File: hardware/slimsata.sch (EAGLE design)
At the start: 2 parts

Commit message: Signaleitungen geroutet
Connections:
- removed net N$1: CON1G$2.GND1, CON1G$2.GND2, CON1G$2.GND3, CON1G$2.GND4, CON1G$2.GND5, CON1G$3.MECH1, CON1G$3.MECH2, CON2G$2.GND1, CON2G$2.GND2, CON2G$3.MECH1, CON2G$3.MECH2, CON2G$3.MECH3
- removed net N$2: CON1G$1.GND1, CON1G$1.GND2, CON1G$1.GND3, CON2G$1.GND1, CON2G$1.GND2, CON2G$1.GND3
- new net GND: CON1G$1.GND1, CON1G$1.GND2, CON1G$1.GND3, CON1G$2.GND1, CON1G$2.GND2, CON1G$2.GND3, CON1G$2.GND4, CON1G$2.GND5, CON1G$3.MECH1, CON1G$3.MECH2, CON2G$1.GND1, CON2G$1.GND2, CON2G$1.GND3, CON2G$2.GND1, CON2G$2.GND2, CON2G$3.MECH1, CON2G$3.MECH2, CON2G$3.MECH3
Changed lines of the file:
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@@
 </busses>
 <nets>
-<net name="N$1" class="0">
-<segment>
-<pinref part="CON1" gate="G$3" pin="MECH2"/>
-<wire x1="30.48" y1="17.78" x2="30.48" y2="15.24" width="0.1524" layer="91"/>
-<wire x1="30.48" y1="15.24" x2="30.48" y2="12.7" width="0.1524" layer="91"/>
-<wire x1="30.48" y1="12.7" x2="30.48" y2="10.16" width="0.1524" layer="91"/>
-<wire x1="30.48" y1="10.16" x2="30.48" y2="7.62" width="0.1524" layer="91"/>
-<wire x1="30.48" y1="7.62" x2="17.78" y2="7.62" width="0.1524" layer="91"/>
-<pinref part="CON1" gate="G$3" pin="MECH1"/>
-<wire x1="17.78" y1="10.16" x2="30.48" y2="10.16" width="0.1524" layer="91"/>
-<junction x="30.48" y="10.16"/>
-<pinref part="CON2" gate="G$3" pin="MECH3"/>
-<wire x1="43.18" y1="12.7" x2="30.48" y2="12.7" width="0.1524" layer="91"/>
-<junction x="30.48" y="12.7"/>
-<pinref part="CON2" gate="G$3" pin="MECH2"/>
-<wire x1="43.18" y1="15.24" x2="30.48" y2="15.24" width="0.1524" layer="91"/>
-<junction x="30.48" y="15.24"/>
-<pinref part="CON2" gate="G$3" pin="MECH1"/>
-<wire x1="43.18" y1="17.78" x2="30.48" y2="17.78" width="0.1524" layer="91"/>
-<pinref part="CON1" gate="G$2" pin="GND1"/>
-<wire x1="17.78" y1="50.8" x2="30.48" y2="50.8" width="0.1524" layer="91"/>
-<wire x1="30.48" y1="50.8" x2="30.48" y2="48.26" width="0.1524" layer="91"/>
-<junction x="30.48" y="17.78"/>
-<pinref part="CON1" gate="G$2" pin="GND2"/>
-<wire x1="30.48" y1="48.26" x2="30.48" y2="45.72" width="0.1524" layer="91"/>
-<wire x1="30.48" y1="45.72" x2="30.48" y2="40.64" width="0.1524" layer="91"/>
-<wire x1="30.48" y1="40.64" x2="30.48" y2="38.1" width="0.1524" layer="91"/>
-<wire x1="30.48" y1="38.1" x2="30.48" y2="35.56" width="0.1524" layer="91"/>
-<wire x1="30.48" y1="35.56" x2="30.48" y2="30.48" width="0.1524" layer="91"/>
-<wire x1="30.48" y1="30.48" x2="30.48" y2="17.78" width="0.1524" layer="91"/>
-<wire x1="17.78" y1="48.26" x2="30.48" y2="48.26" width="0.1524" layer="91"/>
-<junction x="30.48" y="48.26"/>
-<pinref part="CON1" gate="G$2" pin="GND3"/>
-<wire x1="17.78" y1="45.72" x2="30.48" y2="45.72" width="0.1524" layer="91"/>
-<junction x="30.48" y="45.72"/>
-<pinref part="CON1" gate="G$2" pin="GND4"/>
-<wire x1="17.78" y1="35.56" x2="30.48" y2="35.56" width="0.1524" layer="91"/>
-<junction x="30.48" y="35.56"/>
-<pinref part="CON1" gate="G$2" pin="GND5"/>
-<wire x1="17.78" y1="30.48" x2="30.48" y2="30.48" width="0.1524" layer="91"/>
-<junction x="30.48" y="30.48"/>
-<pinref part="CON2" gate="G$2" pin="GND2"/>
-<wire x1="43.18" y1="38.1" x2="30.48" y2="38.1" width="0.1524" layer="91"/>
-<junction x="30.48" y="38.1"/>
-<pinref part="CON2" gate="G$2" pin="GND1"/>
-<wire x1="43.18" y1="40.64" x2="30.48" y2="40.64" width="0.1524" layer="91"/>
-<junction x="30.48" y="40.64"/>
-</segment>
-</net>
-<net name="N$2" class="0">
-<segment>
-<pinref part="CON2" gate="G$1" pin="GND1"/>
-<pinref part="CON1" gate="G$1" pin="GND1"/>
-<wire x1="17.78" y1="81.28" x2="30.48" y2="81.28" width="0.1524" layer="91"/>
-<pinref part="CON1" gate="G$1" pin="GND2"/>
-<pinref part="CON2" gate="G$1" pin="GND2"/>
-<wire x1="30.48" y1="81.28" x2="43.18" y2="81.28" width="0.1524" layer="91"/>
-<wire x1="17.78" y1="73.66" x2="30.48" y2="73.66" width="0.1524" layer="91"/>
-<wire x1="30.48" y1="73.66" x2="43.18" y2="73.66" width="0.1524" layer="91"/>
-<wire x1="30.48" y1="81.28" x2="30.48" y2="73.66" width="0.1524" layer="91"/>
-<junction x="30.48" y="81.28"/>
-<junction x="30.48" y="73.66"/>
-<pinref part="CON1" gate="G$1" pin="GND3"/>
-<pinref part="CON2" gate="G$1" pin="GND3"/>
-<wire x1="17.78" y1="66.04" x2="30.48" y2="66.04" width="0.1524" layer="91"/>
-<wire x1="30.48" y1="66.04" x2="43.18" y2="66.04" width="0.1524" layer="91"/>
-<wire x1="30.48" y1="73.66" x2="30.48" y2="66.04" width="0.1524" layer="91"/>
-<junction x="30.48" y="66.04"/>
-</segment>
-</net>
 <net name="N$5" class="0">
 <segment>
@@
 </segment>
 </net>
+<net name="GND" class="0">
+<segment>
+<pinref part="CON2" gate="G$1" pin="GND1"/>
+<pinref part="CON1" gate="G$1" pin="GND1"/>
+<wire x1="17.78" y1="81.28" x2="30.48" y2="81.28" width="0.1524" layer="91"/>
+<pinref part="CON1" gate="G$1" pin="GND2"/>
+<pinref part="CON2" gate="G$1" pin="GND2"/>
+<wire x1="30.48" y1="81.28" x2="43.18" y2="81.28" width="0.1524" layer="91"/>
+<wire x1="17.78" y1="73.66" x2="30.48" y2="73.66" width="0.1524" layer="91"/>
+<wire x1="30.48" y1="73.66" x2="43.18" y2="73.66" width="0.1524" layer="91"/>
+<wire x1="30.48" y1="81.28" x2="30.48" y2="73.66" width="0.1524" layer="91"/>
+<junction x="30.48" y="81.28"/>
+<junction x="30.48" y="73.66"/>
+<pinref part="CON1" gate="G$1" pin="GND3"/>
+<pinref part="CON2" gate="G$1" pin="GND3"/>
+<wire x1="17.78" y1="66.04" x2="30.48" y2="66.04" width="0.1524" layer="91"/>
+<wire x1="30.48" y1="66.04" x2="43.18" y2="66.04" width="0.1524" layer="91"/>
+<wire x1="30.48" y1="73.66" x2="30.48" y2="66.04" width="0.1524" layer="91"/>
+<junction x="30.48" y="66.04"/>
+<pinref part="CON1" gate="G$3" pin="MECH2"/>
+<wire x1="30.48" y1="17.78" x2="30.48" y2="15.24" width="0.1524" layer="91"/>
+<wire x1="30.48" y1="15.24" x2="30.48" y2="12.7" width="0.1524" layer="91"/>
+<wire x1="30.48" y1="12.7" x2="30.48" y2="10.16" width="0.1524" layer="91"/>
+<wire x1="30.48" y1="10.16" x2="30.48" y2="7.62" width="0.1524" layer="91"/>
+<wire x1="30.48" y1="7.62" x2="17.78" y2="7.62" width="0.1524" layer="91"/>
+<pinref part="CON1" gate="G$3" pin="MECH1"/>
+<wire x1="17.78" y1="10.16" x2="30.48" y2="10.16" width="0.1524" layer="91"/>
+<junction x="30.48" y="10.16"/>
+<pinref part="CON2" gate="G$3" pin="MECH3"/>
+<wire x1="43.18" y1="12.7" x2="30.48" y2="12.7" width="0.1524" layer="91"/>
+<junction x="30.48" y="12.7"/>
+<pinref part="CON2" gate="G$3" pin="MECH2"/>
+<wire x1="43.18" y1="15.24" x2="30.48" y2="15.24" width="0.1524" layer="91"/>
+<junction x="30.48" y="15.24"/>
+<pinref part="CON2" gate="G$3" pin="MECH1"/>
+<wire x1="43.18" y1="17.78" x2="30.48" y2="17.78" width="0.1524" layer="91"/>
+<pinref part="CON1" gate="G$2" pin="GND1"/>
+<wire x1="17.78" y1="50.8" x2="30.48" y2="50.8" width="0.1524" layer="91"/>
+<wire x1="30.48" y1="50.8" x2="30.48" y2="48.26" width="0.1524" layer="91"/>
+<junction x="30.48" y="17.78"/>
+<pinref part="CON1" gate="G$2" pin="GND2"/>
+<wire x1="30.48" y1="48.26" x2="30.48" y2="45.72" width="0.1524" layer="91"/>
+<wire x1="30.48" y1="45.72" x2="30.48" y2="40.64" width="0.1524" layer="91"/>
+<wire x1="30.48" y1="40.64" x2="30.48" y2="38.1" width="0.1524" layer="91"/>
+<wire x1="30.48" y1="38.1" x2="30.48" y2="35.56" width="0.1524" layer="91"/>
+<wire x1="30.48" y1="35.56" x2="30.48" y2="30.48" width="0.1524" layer="91"/>
+<wire x1="30.48" y1="30.48" x2="30.48" y2="17.78" width="0.1524" layer="91"/>
+<wire x1="17.78" y1="48.26" x2="30.48" y2="48.26" width="0.1524" layer="91"/>
+<junction x="30.48" y="48.26"/>
+<pinref part="CON1" gate="G$2" pin="GND3"/>
+<wire x1="17.78" y1="45.72" x2="30.48" y2="45.72" width="0.1524" layer="91"/>
+<junction x="30.48" y="45.72"/>
+<pinref part="CON1" gate="G$2" pin="GND4"/>
+<wire x1="17.78" y1="35.56" x2="30.48" y2="35.56" width="0.1524" layer="91"/>
+<junction x="30.48" y="35.56"/>
+<pinref part="CON1" gate="G$2" pin="GND5"/>
+<wire x1="17.78" y1="30.48" x2="30.48" y2="30.48" width="0.1524" layer="91"/>
+<junction x="30.48" y="30.48"/>
+<pinref part="CON2" gate="G$2" pin="GND2"/>
+<wire x1="43.18" y1="38.1" x2="30.48" y2="38.1" width="0.1524" layer="91"/>
+<junction x="30.48" y="38.1"/>
+<pinref part="CON2" gate="G$2" pin="GND1"/>
+<wire x1="43.18" y1="40.64" x2="30.48" y2="40.64" width="0.1524" layer="91"/>
+<junction x="30.48" y="40.64"/>
+<wire x1="30.48" y1="66.04" x2="30.48" y2="50.8" width="0.1524" layer="91"/>
+<junction x="30.48" y="50.8"/>
+</segment>
+</net>

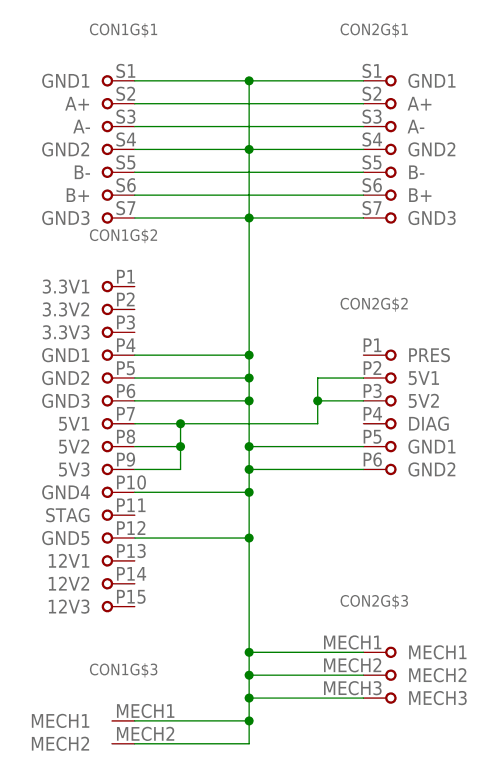
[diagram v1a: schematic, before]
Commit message: Stecker Molex 67492 platziert, Platinenumrisse angepasst
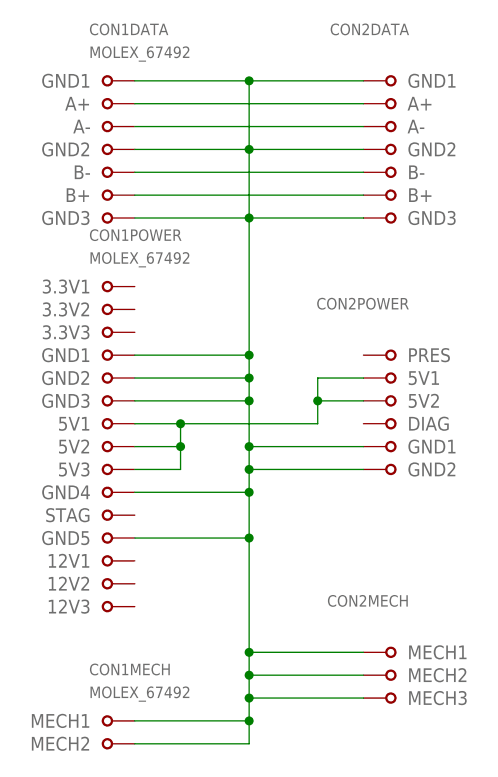
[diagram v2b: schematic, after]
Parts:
- CON1: value (none) -> MOLEX_67492; device sata:MOLEX_47018 -> sata:MOLEX_67492
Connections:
- net GND: now also CON1DATA.GND1, CON1DATA.GND2, CON1DATA.GND3, CON1MECH.MECH1, CON1MECH.MECH2, CON1POWER.GND1, CON1POWER.GND2, CON1POWER.GND3, CON1POWER.GND4, CON1POWER.GND5, CON2DATA.GND1, CON2DATA.GND2, CON2DATA.GND3, CON2MECH.MECH1, CON2MECH.MECH2, CON2MECH.MECH3, CON2POWER.GND1, CON2POWER.GND2; no longer CON1G$1.GND1, CON1G$1.GND2, CON1G$1.GND3, CON1G$2.GND1, CON1G$2.GND2, CON1G$2.GND3, CON1G$2.GND4, CON1G$2.GND5, CON1G$3.MECH1, CON1G$3.MECH2, CON2G$1.GND1, CON2G$1.GND2, CON2G$1.GND3, CON2G$2.GND1, CON2G$2.GND2, CON2G$3.MECH1, CON2G$3.MECH2, CON2G$3.MECH3
- net N$3: now also CON1POWER.5V1, CON1POWER.5V2, CON1POWER.5V3, CON2POWER.5V1, CON2POWER.5V2; no longer CON1G$2.5V1, CON1G$2.5V2, CON1G$2.5V3, CON2G$2.5V1, CON2G$2.5V2
- net N$5: now also CON1DATA.A+, CON2DATA.A+; no longer CON1G$1.A+, CON2G$1.A+
- net N$6: now also CON1DATA.A-, CON2DATA.A-; no longer CON1G$1.A-, CON2G$1.A-
- net N$7: now also CON1DATA.B-, CON2DATA.B-; no longer CON1G$1.B-, CON2G$1.B-
- net N$8: now also CON1DATA.B+, CON2DATA.B+; no longer CON1G$1.B+, CON2G$1.B+
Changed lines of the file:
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@@
 </classes>
 <parts>
-<part name="CON1" library="sata" deviceset="MOLEX_47018" device=""/>
+<part name="CON1" library="sata" deviceset="MOLEX_67492" device=""/>
 <part name="CON2" library="sata" deviceset="MOLEX_47300-100X/101X" device=""/>
 </parts>
@@
 </plain>
 <instances>
-<instance part="CON1" gate="G$1" x="17.78" y="73.66"/>
-<instance part="CON1" gate="G$2" x="17.78" y="40.64"/>
-<instance part="CON1" gate="G$3" x="17.78" y="10.16"/>
-<instance part="CON2" gate="G$1" x="43.18" y="73.66" rot="MR0"/>
-<instance part="CON2" gate="G$2" x="43.18" y="43.18" rot="MR0"/>
-<instance part="CON2" gate="G$3" x="43.18" y="15.24" rot="MR0"/>
+<instance part="CON1" gate="DATA" x="17.78" y="73.66"/>
+<instance part="CON1" gate="POWER" x="17.78" y="40.64"/>
+<instance part="CON1" gate="MECH" x="17.78" y="10.16"/>
+<instance part="CON2" gate="DATA" x="43.18" y="73.66" rot="MR0"/>
+<instance part="CON2" gate="POWER" x="43.18" y="43.18" rot="MR0"/>
+<instance part="CON2" gate="MECH" x="43.18" y="15.24" rot="MR0"/>
 </instances>
 <busses>
@@
 <net name="N$5" class="0">
 <segment>
-<pinref part="CON1" gate="G$1" pin="A+"/>
-<pinref part="CON2" gate="G$1" pin="A+"/>
+<pinref part="CON1" gate="DATA" pin="A+"/>
+<pinref part="CON2" gate="DATA" pin="A+"/>
 <wire x1="17.78" y1="78.74" x2="43.18" y2="78.74" width="0.1524" layer="91"/>
 </segment>
@@
 <net name="N$6" class="0">
 <segment>
-<pinref part="CON1" gate="G$1" pin="A-"/>
-<pinref part="CON2" gate="G$1" pin="A-"/>
+<pinref part="CON1" gate="DATA" pin="A-"/>
+<pinref part="CON2" gate="DATA" pin="A-"/>
 <wire x1="17.78" y1="76.2" x2="43.18" y2="76.2" width="0.1524" layer="91"/>
 </segment>
@@
 <net name="N$7" class="0">
 <segment>
-<pinref part="CON1" gate="G$1" pin="B-"/>
-<pinref part="CON2" gate="G$1" pin="B-"/>
+<pinref part="CON1" gate="DATA" pin="B-"/>
+<pinref part="CON2" gate="DATA" pin="B-"/>
 <wire x1="17.78" y1="71.12" x2="43.18" y2="71.12" width="0.1524" layer="91"/>
 </segment>
@@
 <net name="N$8" class="0">
 <segment>
-<pinref part="CON1" gate="G$1" pin="B+"/>
-<pinref part="CON2" gate="G$1" pin="B+"/>
+<pinref part="CON1" gate="DATA" pin="B+"/>
+<pinref part="CON2" gate="DATA" pin="B+"/>
 <wire x1="17.78" y1="68.58" x2="43.18" y2="68.58" width="0.1524" layer="91"/>
 </segment>
@@
 <net name="N$3" class="0">
 <segment>
-<pinref part="CON1" gate="G$2" pin="5V1"/>
+<pinref part="CON1" gate="POWER" pin="5V1"/>
 <wire x1="17.78" y1="43.18" x2="22.86" y2="43.18" width="0.1524" layer="91"/>
 <wire x1="22.86" y1="43.18" x2="22.86" y2="40.64" width="0.1524" layer="91"/>
-<pinref part="CON1" gate="G$2" pin="5V3"/>
+<pinref part="CON1" gate="POWER" pin="5V3"/>
 <wire x1="22.86" y1="40.64" x2="22.86" y2="38.1" width="0.1524" layer="91"/>
 <wire x1="22.86" y1="38.1" x2="17.78" y2="38.1" width="0.1524" layer="91"/>
-<pinref part="CON1" gate="G$2" pin="5V2"/>
+<pinref part="CON1" gate="POWER" pin="5V2"/>
 <wire x1="17.78" y1="40.64" x2="22.86" y2="40.64" width="0.1524" layer="91"/>
 <junction x="22.86" y="40.64"/>
@@
 <wire x1="38.1" y1="43.18" x2="38.1" y2="45.72" width="0.1524" layer="91"/>
 <junction x="22.86" y="43.18"/>
-<pinref part="CON2" gate="G$2" pin="5V1"/>
+<pinref part="CON2" gate="POWER" pin="5V1"/>
 <wire x1="38.1" y1="45.72" x2="38.1" y2="48.26" width="0.1524" layer="91"/>
 <wire x1="38.1" y1="48.26" x2="43.18" y2="48.26" width="0.1524" layer="91"/>
-<pinref part="CON2" gate="G$2" pin="5V2"/>
+<pinref part="CON2" gate="POWER" pin="5V2"/>
 <wire x1="43.18" y1="45.72" x2="38.1" y2="45.72" width="0.1524" layer="91"/>
 <junction x="38.1" y="45.72"/>
@@
 <net name="GND" class="0">
 <segment>
-<pinref part="CON2" gate="G$1" pin="GND1"/>
-<pinref part="CON1" gate="G$1" pin="GND1"/>
+<pinref part="CON2" gate="DATA" pin="GND1"/>
+<pinref part="CON1" gate="DATA" pin="GND1"/>
 <wire x1="17.78" y1="81.28" x2="30.48" y2="81.28" width="0.1524" layer="91"/>
-<pinref part="CON1" gate="G$1" pin="GND2"/>
-<pinref part="CON2" gate="G$1" pin="GND2"/>
+<pinref part="CON1" gate="DATA" pin="GND2"/>
+<pinref part="CON2" gate="DATA" pin="GND2"/>
 <wire x1="30.48" y1="81.28" x2="43.18" y2="81.28" width="0.1524" layer="91"/>
 <wire x1="17.78" y1="73.66" x2="30.48" y2="73.66" width="0.1524" layer="91"/>
@@
 <junction x="30.48" y="81.28"/>
 <junction x="30.48" y="73.66"/>
-<pinref part="CON1" gate="G$1" pin="GND3"/>
-<pinref part="CON2" gate="G$1" pin="GND3"/>
+<pinref part="CON1" gate="DATA" pin="GND3"/>
+<pinref part="CON2" gate="DATA" pin="GND3"/>
 <wire x1="17.78" y1="66.04" x2="30.48" y2="66.04" width="0.1524" layer="91"/>
 <wire x1="30.48" y1="66.04" x2="43.18" y2="66.04" width="0.1524" layer="91"/>
 <wire x1="30.48" y1="73.66" x2="30.48" y2="66.04" width="0.1524" layer="91"/>
 <junction x="30.48" y="66.04"/>
-<pinref part="CON1" gate="G$3" pin="MECH2"/>
+<pinref part="CON1" gate="MECH" pin="MECH2"/>
 <wire x1="30.48" y1="17.78" x2="30.48" y2="15.24" width="0.1524" layer="91"/>
 <wire x1="30.48" y1="15.24" x2="30.48" y2="12.7" width="0.1524" layer="91"/>
@@
 <wire x1="30.48" y1="10.16" x2="30.48" y2="7.62" width="0.1524" layer="91"/>
 <wire x1="30.48" y1="7.62" x2="17.78" y2="7.62" width="0.1524" layer="91"/>
-<pinref part="CON1" gate="G$3" pin="MECH1"/>
+<pinref part="CON1" gate="MECH" pin="MECH1"/>
 <wire x1="17.78" y1="10.16" x2="30.48" y2="10.16" width="0.1524" layer="91"/>
 <junction x="30.48" y="10.16"/>
-<pinref part="CON2" gate="G$3" pin="MECH3"/>
+<pinref part="CON2" gate="MECH" pin="MECH3"/>
 <wire x1="43.18" y1="12.7" x2="30.48" y2="12.7" width="0.1524" layer="91"/>
 <junction x="30.48" y="12.7"/>
-<pinref part="CON2" gate="G$3" pin="MECH2"/>
+<pinref part="CON2" gate="MECH" pin="MECH2"/>
 <wire x1="43.18" y1="15.24" x2="30.48" y2="15.24" width="0.1524" layer="91"/>
 <junction x="30.48" y="15.24"/>
-<pinref part="CON2" gate="G$3" pin="MECH1"/>
+<pinref part="CON2" gate="MECH" pin="MECH1"/>
 <wire x1="43.18" y1="17.78" x2="30.48" y2="17.78" width="0.1524" layer="91"/>
-<pinref part="CON1" gate="G$2" pin="GND1"/>
+<pinref part="CON1" gate="POWER" pin="GND1"/>
 <wire x1="17.78" y1="50.8" x2="30.48" y2="50.8" width="0.1524" layer="91"/>
 <wire x1="30.48" y1="50.8" x2="30.48" y2="48.26" width="0.1524" layer="91"/>
 <junction x="30.48" y="17.78"/>
-<pinref part="CON1" gate="G$2" pin="GND2"/>
+<pinref part="CON1" gate="POWER" pin="GND2"/>
 <wire x1="30.48" y1="48.26" x2="30.48" y2="45.72" width="0.1524" layer="91"/>
 <wire x1="30.48" y1="45.72" x2="30.48" y2="40.64" width="0.1524" layer="91"/>
@@
 <wire x1="17.78" y1="48.26" x2="30.48" y2="48.26" width="0.1524" layer="91"/>
 <junction x="30.48" y="48.26"/>
-<pinref part="CON1" gate="G$2" pin="GND3"/>
+<pinref part="CON1" gate="POWER" pin="GND3"/>
 <wire x1="17.78" y1="45.72" x2="30.48" y2="45.72" width="0.1524" layer="91"/>
 <junction x="30.48" y="45.72"/>
-<pinref part="CON1" gate="G$2" pin="GND4"/>
+<pinref part="CON1" gate="POWER" pin="GND4"/>
 <wire x1="17.78" y1="35.56" x2="30.48" y2="35.56" width="0.1524" layer="91"/>
 <junction x="30.48" y="35.56"/>
-<pinref part="CON1" gate="G$2" pin="GND5"/>
+<pinref part="CON1" gate="POWER" pin="GND5"/>
 <wire x1="17.78" y1="30.48" x2="30.48" y2="30.48" width="0.1524" layer="91"/>
 <junction x="30.48" y="30.48"/>
-<pinref part="CON2" gate="G$2" pin="GND2"/>
+<pinref part="CON2" gate="POWER" pin="GND2"/>
 <wire x1="43.18" y1="38.1" x2="30.48" y2="38.1" width="0.1524" layer="91"/>
 <junction x="30.48" y="38.1"/>
-<pinref part="CON2" gate="G$2" pin="GND1"/>
+<pinref part="CON2" gate="POWER" pin="GND1"/>
 <wire x1="43.18" y1="40.64" x2="30.48" y2="40.64" width="0.1524" layer="91"/>
 <junction x="30.48" y="40.64"/>

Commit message: Abstände Datenleitungen <-> GND auf 20 mil vergrössert.
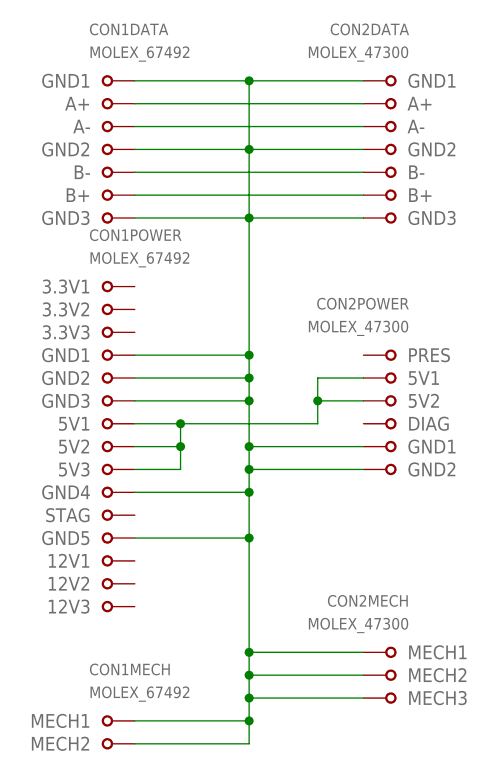
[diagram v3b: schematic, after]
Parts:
- CON2: value (none) -> MOLEX_47300
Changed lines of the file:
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@@
 <class number="0" name="default" width="0" drill="0">
+</class>
+<class number="1" name="data" width="0" drill="0">
+</class>
+<class number="2" name="gnd" width="0" drill="0">
+<clearance class="1" value="0.508"/>
 </class>
 </classes>
 <parts>
 <part name="CON1" library="sata" deviceset="MOLEX_67492" device=""/>
-<part name="CON2" library="sata" deviceset="MOLEX_47300-100X/101X" device=""/>
+<part name="CON2" library="sata" deviceset="MOLEX_47300-100X/101X" device="" value="MOLEX_47300"/>
 </parts>
 <sheets>
@@
 </busses>
 <nets>
-<net name="N$5" class="0">
+<net name="N$5" class="1">
 <segment>
 <pinref part="CON1" gate="DATA" pin="A+"/>
@@
 </segment>
 </net>
-<net name="N$6" class="0">
+<net name="N$6" class="1">
 <segment>
 <pinref part="CON1" gate="DATA" pin="A-"/>
@@
 </segment>
 </net>
-<net name="N$7" class="0">
+<net name="N$7" class="1">
 <segment>
 <pinref part="CON1" gate="DATA" pin="B-"/>
@@
 </segment>
 </net>
-<net name="N$8" class="0">
+<net name="N$8" class="1">
 <segment>
 <pinref part="CON1" gate="DATA" pin="B+"/>
@@
 </segment>
 </net>
-<net name="GND" class="0">
+<net name="GND" class="2">
 <segment>
 <pinref part="CON2" gate="DATA" pin="GND1"/>
